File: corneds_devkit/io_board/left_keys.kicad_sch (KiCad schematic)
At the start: 64 parts, among them SW1 SW_Push, SW10 SW_Push, SW11 SW_Push, SW12 SW_Push, SW13 SW_Push, SW15 SW_Push, SW17 SW_Push, SW19 SW_Push, SW2 SW_Push, SW20 SW_Push, SW21 SW_Push, SW22 SW_Push, SW23 SW_Push, SW24 SW_Push, SW3 SW_Push, SW4 SW_Push, SW5 SW_Push, SW6 SW_Push, SW7 SW_Push, SW8 SW_Push, SW9 SW_Push

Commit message: finished mouse and key boards
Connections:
- net lclick_led_di: now reaches D38.1 (DO)
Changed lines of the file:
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@@
+	(wire
+		(pts
+			(xy 163.83 142.24) (xy 166.37 142.24)
+		)
+		(stroke
+			(width 0)
+			(type default)
+		)
+	)
 	(wire
 		(pts
@@
 				(hide yes)
 			)
+		)
+	)
+	(global_label "lclick_led_di"
+		(shape input)
+		(at 163.83 142.24 180)
+		(fields_autoplaced yes)
+		(effects
+			(font
+				(size 1.27 1.27)
+			)
+			(justify right)
+		)
+		(property "Intersheetrefs" "${INTERSHEET_REFS}"
+			(at 149.1125 142.24 0)
+			(effects
+				(font
+					(size 1.27 1.27)
+				)
+				(justify right)
+				(hide yes)
+			)

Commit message: finished schematic for io board
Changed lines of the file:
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@@
 	)
 	(junction
-		(at 255.27 152.4)
-		(diameter 0)
-		(color 0 0 0 0)
-	)
-	(junction
 		(at 229.87 152.4)
 		(diameter 0)
@@
 	)
 	(junction
-		(at 63.5 26.67)
-		(diameter 0)
-		(color 0 0 0 0)
-	)
-	(junction
 		(at 140.97 58.42)
 		(diameter 0)
@@
 		)
 	)
+	(global_label "VDDL"
+		(shape input)
+		(at 63.5 26.67 90)
+		(fields_autoplaced yes)
+		(effects
+			(font
+				(size 1.27 1.27)
+			)
+			(justify left)
+		)
+		(property "Intersheetrefs" "${INTERSHEET_REFS}"
+			(at 63.5 19.0281 90)
+			(effects
+				(font
+					(size 1.27 1.27)
+				)
+				(justify left)
+				(hide yes)
+			)
+		)
+	)
 	(global_label "key_t"
 		(shape input)
@@
 		)
 	)
+	(global_label "GNDL"
+		(shape input)
+		(at 255.27 152.4 270)
+		(fields_autoplaced yes)
+		(effects
+			(font
+				(size 1.27 1.27)
+			)
+			(justify right)
+		)
+		(property "Intersheetrefs" "${INTERSHEET_REFS}"
+			(at 255.27 160.2838 90)
+			(effects
+				(font
+					(size 1.27 1.27)
+				)
+				(justify right)
+				(hide yes)
+			)
+		)
+	)
 	(global_label "key_d"
 		(shape input)
@@
 	)
 	(symbol
-		(lib_id "power:VDD")
-		(at 63.5 26.67 0)
-		(unit 1)
-		(exclude_from_sim no)
-		(in_bom yes)
-		(on_board yes)
-		(dnp no)
-		(fields_autoplaced yes)
-		(property "Reference" "#PWR01"
-			(at 63.5 30.48 0)
-			(effects
-				(font
-					(size 1.27 1.27)
-				)
-				(hide yes)
-			)
-		)
-		(property "Value" "VDDL"
-			(at 63.5 21.59 0)
-			(effects
-				(font
-					(size 1.27 1.27)
-				)
-			)
-		)
-		(property "Footprint" ""
-			(at 63.5 26.67 0)
-			(effects
-				(font
-					(size 1.27 1.27)
-				)
-				(hide yes)
-			)
-		)
-		(property "Datasheet" ""
-			(at 63.5 26.67 0)
-			(effects
-				(font
-					(size 1.27 1.27)
-				)
-				(hide yes)
-			)
-		)
-		(property "Description" "Power symbol creates a global label with name \"VDD\""
-			(at 63.5 26.67 0)
-			(effects
-				(font
-					(size 1.27 1.27)
-				)
-				(hide yes)
-			)
-		)
-		(pin "1"
-		)
-		(instances
-			(project "io_board"
-				(path "/244b6d6b-132d-4d50-ae86-e41103b29008/035ff8de-23b0-4e40-a4d6-13420d9ceca3"
-					(reference "#PWR01")
-					(unit 1)
-				)
-			)
-		)
-	)
-	(symbol
 		(lib_id "Diode:1N4148W")
 		(at 156.21 100.33 180)
@@
 					(unit 1)
 				)
-			)
-		)
-	)
-	(symbol
-		(lib_id "power:GND")
-		(at 255.27 152.4 0)
-		(unit 1)
-		(exclude_from_sim no)
-		(in_bom yes)
-		(on_board yes)
-		(dnp no)
-		(fields_autoplaced yes)
-		(property "Reference" "#PWR02"
-			(at 255.27 158.75 0)
-			(effects
-				(font
-					(size 1.27 1.27)
-				)
-				(hide yes)
-			)
-		)
-		(property "Value" "GNDL"
-			(at 255.27 157.48 0)
-			(effects
-				(font
-					(size 1.27 1.27)
-				)
-			)
-		)
-		(property "Footprint" ""
-			(at 255.27 152.4 0)
-			(effects
-				(font
-					(size 1.27 1.27)
-				)
-				(hide yes)
-			)
-		)
-		(property "Datasheet" ""
-			(at 255.27 152.4 0)
-			(effects
-				(font
-					(size 1.27 1.27)
-				)
-				(hide yes)
-			)
-		)
-		(property "Description" "Power symbol creates a global label with name \"GND\" , ground"
-			(at 255.27 152.4 0)
-			(effects
-				(font
-					(size 1.27 1.27)
-				)
-				(hide yes)
-			)
-		)
-		(pin "1"
-		)
-		(instances
-			(project "io_board"
-				(path "/244b6d6b-132d-4d50-ae86-e41103b29008/035ff8de-23b0-4e40-a4d6-13420d9ceca3"
-					(reference "#PWR02")
-					(unit 1)
-				)

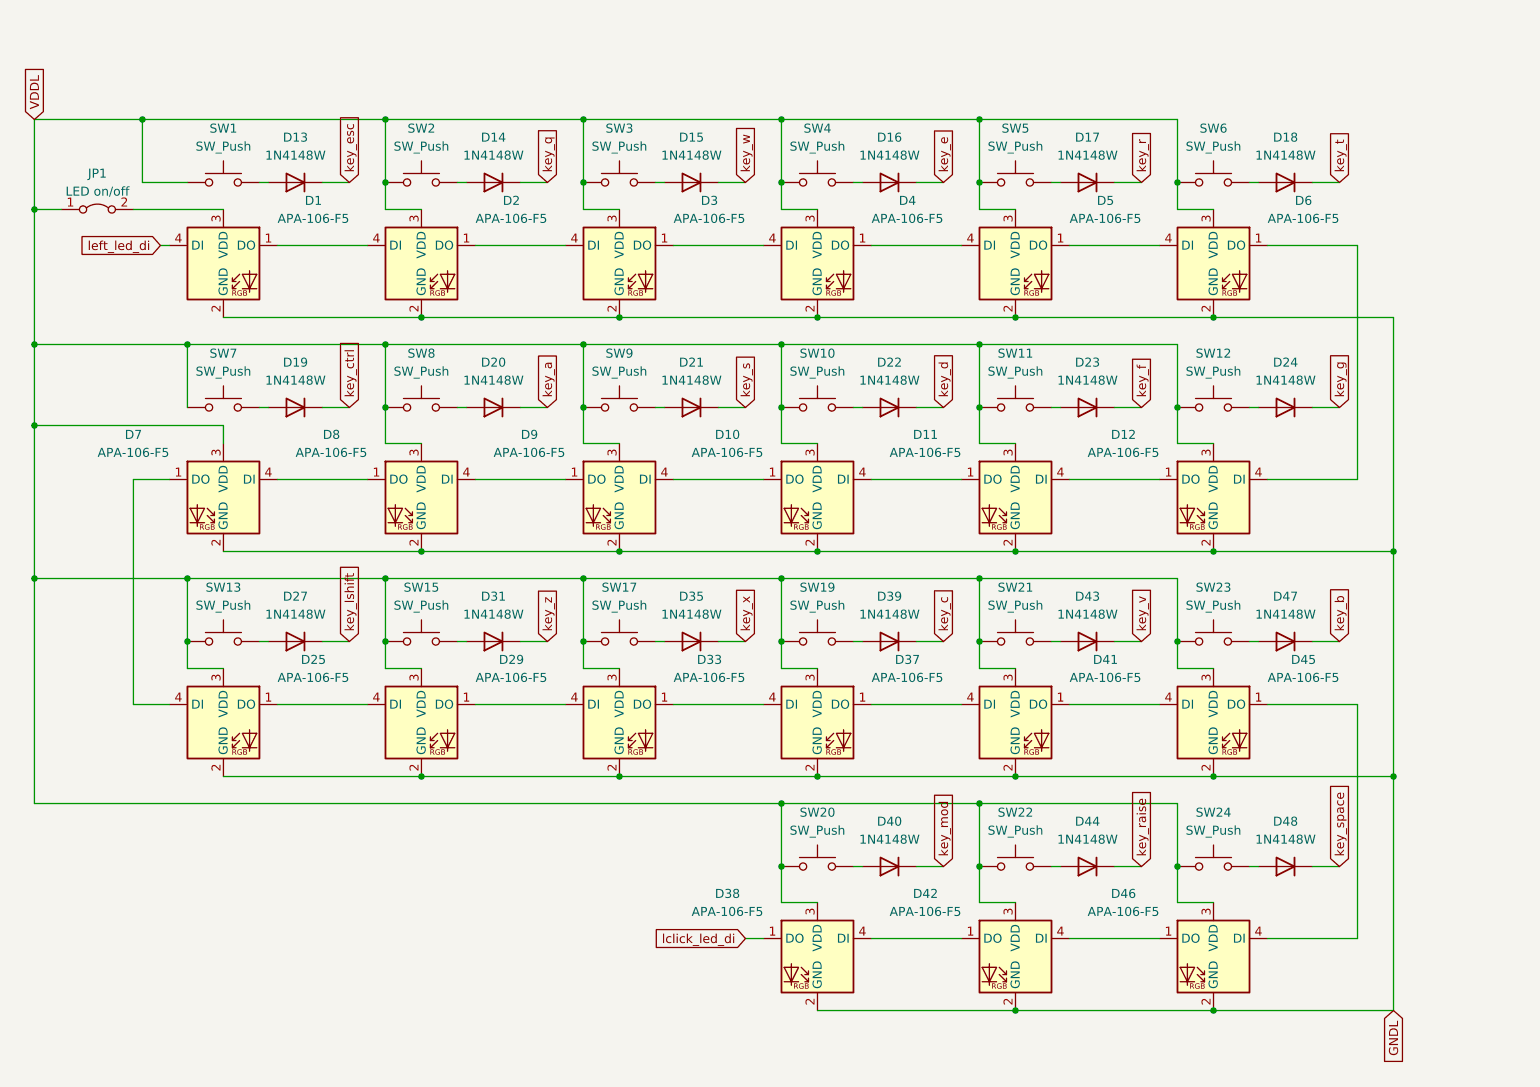
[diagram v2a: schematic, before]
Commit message: re-routed io board with keypad IC
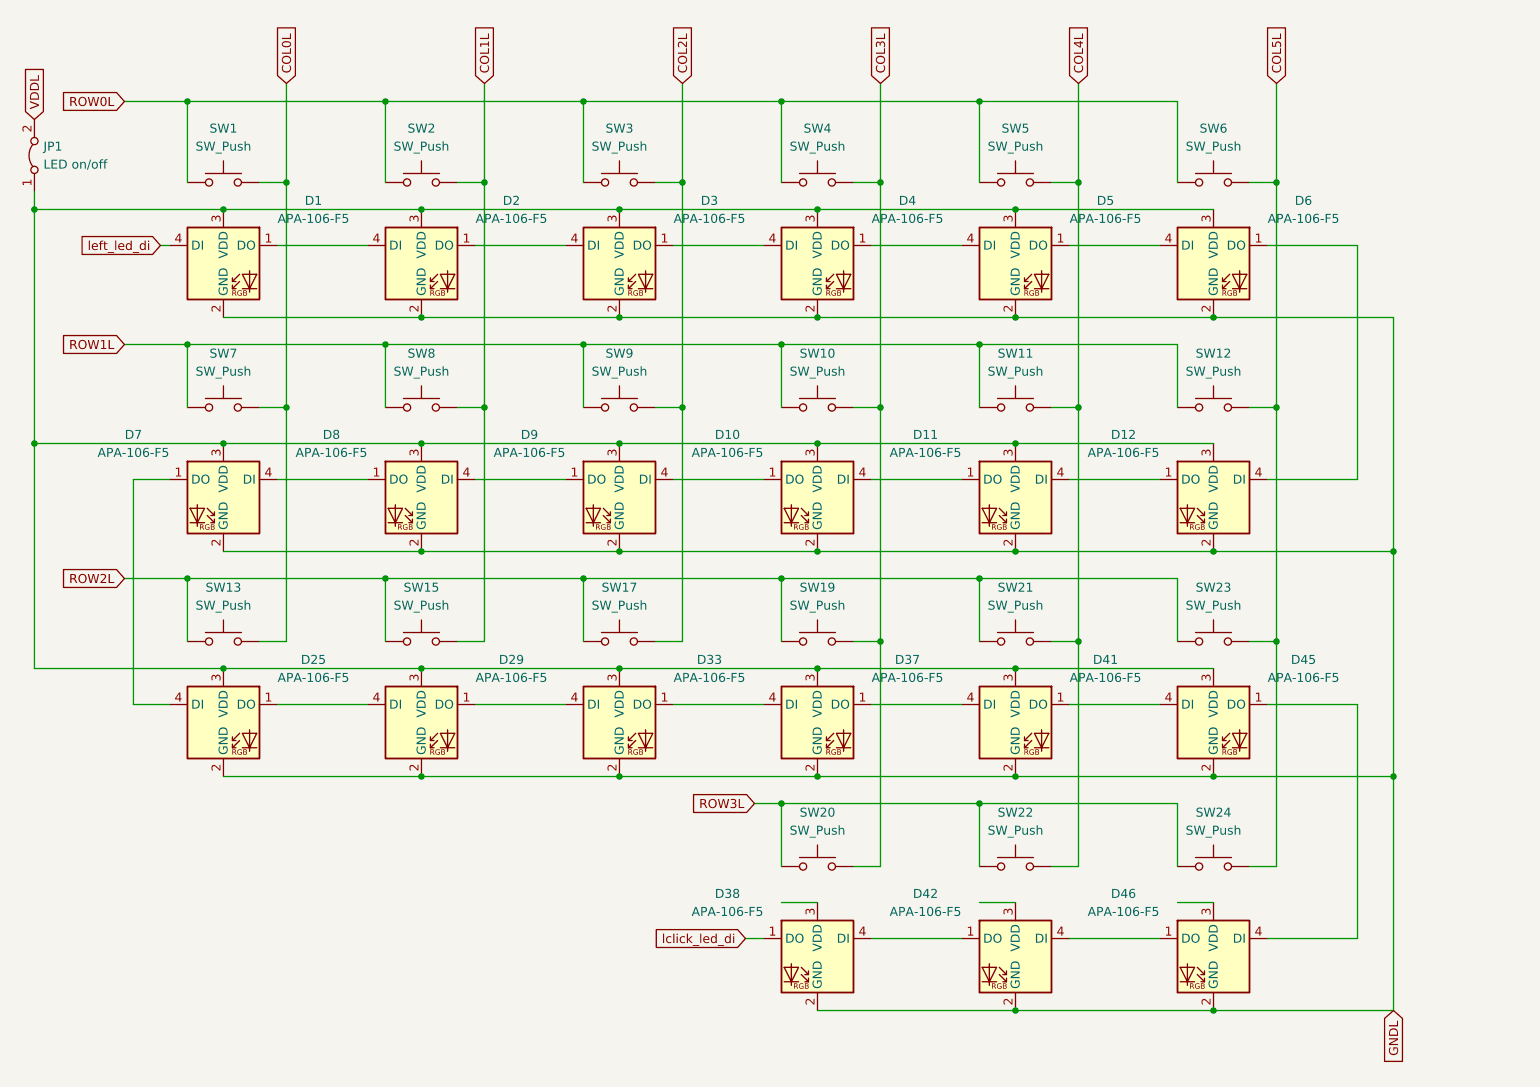
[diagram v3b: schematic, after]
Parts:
- removed D13, D14, D15, D16, D17, D18, D19, D20, D21, D22, D23, D24, D27, D31, D35, D39, D40, D43, D44, D47, D48: 1N4148W, Diode_SMD:D_SOD-123, symbol Diode:1N4148W
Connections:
- net VDDL: now also JP1.2 (B); no longer D10.3 (VDD), D11.3 (VDD), D12.3 (VDD), D2.3 (VDD), D25.3 (VDD), D29.3 (VDD), D3.3 (VDD), D33.3 (VDD), D37.3 (VDD), D38.3 (VDD), D4.3 (VDD), D41.3 (VDD), D42.3 (VDD), D45.3 (VDD), D46.3 (VDD), D5.3 (VDD), D6.3 (VDD), D7.3 (VDD), D8.3 (VDD), D9.3 (VDD), JP1.1 (A), SW1.1, SW10.1, SW11.1, SW12.1, SW13.1, SW15.1, SW17.1, SW19.1, SW2.1, SW20.1, SW21.1, SW22.1, SW23.1, SW24.1, SW3.1, SW4.1, SW5.1, SW6.1, SW7.1, SW8.1, SW9.1
- net COL4L: now reaches SW21.2
- net COL4L: now also SW11.2, SW22.2, SW5.2
- net COL5L: now reaches SW6.2
- net COL5L: now also SW12.2, SW23.2, SW24.2
- net COL3L: now reaches SW20.2
- net COL3L: now also SW10.2, SW19.2, SW4.2
- net at D1.3 (VDD): now also D10.3 (VDD), D11.3 (VDD), D12.3 (VDD), D2.3 (VDD), D25.3 (VDD), D29.3 (VDD), D3.3 (VDD), D33.3 (VDD), D37.3 (VDD), D4.3 (VDD), D41.3 (VDD), D45.3 (VDD), D5.3 (VDD), D6.3 (VDD), D7.3 (VDD), D8.3 (VDD), D9.3 (VDD), JP1.1 (A); no longer JP1.2 (B)
- net COL1L: now reaches SW8.2
- net COL1L: now also SW15.2, SW2.2
- net COL2L: now reaches SW3.2
- net COL2L: now also SW17.2, SW9.2
- net COL0L: now reaches SW7.2
- net COL0L: now also SW1.2, SW13.2
- new net ROW0L: SW1.1, SW2.1, SW3.1, SW4.1, SW5.1, SW6.1
- new net ROW1L: SW10.1, SW11.1, SW12.1, SW7.1, SW8.1, SW9.1
- new net ROW2L: SW13.1, SW15.1, SW17.1, SW19.1, SW21.1, SW23.1
- new net ROW3L: SW20.1, SW22.1, SW24.1
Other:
- moved on the sheet: JP1

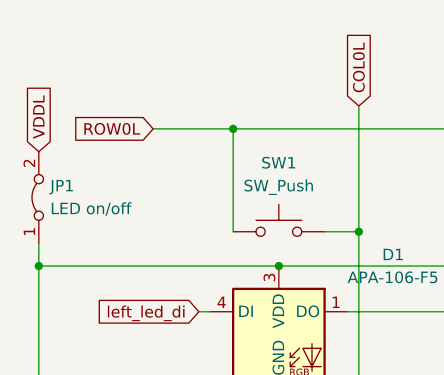
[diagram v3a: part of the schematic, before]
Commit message: added switch footprint, io sch, and keypad IC footprint. Need to find new LEDs and make joystick footprint
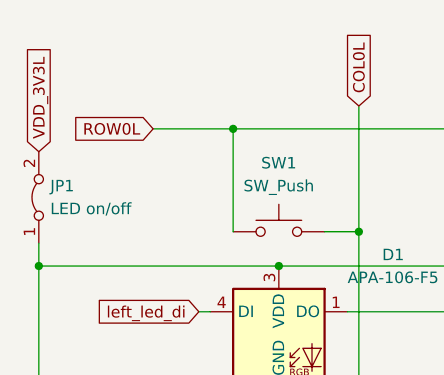
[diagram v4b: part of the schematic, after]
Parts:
- SW1, SW10, SW11, SW12, SW13, SW15, SW17, SW19, SW2, SW20, SW21, SW22, SW23, SW24, SW3, SW4, SW5, SW6, SW7, SW8, SW9: footprint (none) -> key-switches:SW_Gateron_LowProfile_HotSwap_THT
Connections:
- net VDDL renamed VDD_3V3L
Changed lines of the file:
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@@
 		)
 	)
-	(global_label "VDDL"
+	(global_label "VDD_3V3L"
 		(shape input)
 		(at 63.5 26.67 90)
@@
 		)
 		(property "Intersheetrefs" "${INTERSHEET_REFS}"
-			(at 63.5 19.0281 90)
+			(at 63.5 14.5529 90)
 			(effects
 				(font
@@
 			)
 		)
-		(property "Footprint" ""
+		(property "Footprint" "key-switches:SW_Gateron_LowProfile_HotSwap_THT"
 			(at 201.93 95.25 0)
 			(effects
@@
 			)
 		)
-		(property "Footprint" ""
+		(property "Footprint" "key-switches:SW_Gateron_LowProfile_HotSwap_THT"
 			(at 229.87 30.48 0)
 			(effects
@@
 			)
 		)
-		(property "Footprint" ""
+		(property "Footprint" "key-switches:SW_Gateron_LowProfile_HotSwap_THT"
 			(at 173.99 127 0)
 			(effects
@@
 			)
 		)
-		(property "Footprint" ""
+		(property "Footprint" "key-switches:SW_Gateron_LowProfile_HotSwap_THT"
 			(at 173.99 62.23 0)
 			(effects
@@
 			)
 		)
-		(property "Footprint" ""
+		(property "Footprint" "key-switches:SW_Gateron_LowProfile_HotSwap_THT"
 			(at 118.11 62.23 0)
 			(effects
@@
 			)
 		)
-		(property "Footprint" ""
+		(property "Footprint" "key-switches:SW_Gateron_LowProfile_HotSwap_THT"
 			(at 173.99 95.25 0)
 			(effects
@@
 			)
 		)
-		(property "Footprint" ""
+		(property "Footprint" "key-switches:SW_Gateron_LowProfile_HotSwap_THT"
 			(at 229.87 95.25 0)
 			(effects
@@
 			)
 		)
-		(property "Footprint" ""
+		(property "Footprint" "key-switches:SW_Gateron_LowProfile_HotSwap_THT"
 			(at 90.17 62.23 0)
 			(effects
@@
 			)
 		)
-		(property "Footprint" ""
+		(property "Footprint" "key-switches:SW_Gateron_LowProfile_HotSwap_THT"
 			(at 90.17 30.48 0)
 			(effects
@@
 			)
 		)
-		(property "Footprint" ""
+		(property "Footprint" "key-switches:SW_Gateron_LowProfile_HotSwap_THT"
 			(at 229.87 62.23 0)
 			(effects
@@
 			)
 		)
-		(property "Footprint" ""
+		(property "Footprint" "key-switches:SW_Gateron_LowProfile_HotSwap_THT"
 			(at 173.99 30.48 0)
 			(effects
@@
 			)
 		)
-		(property "Footprint" ""
+		(property "Footprint" "key-switches:SW_Gateron_LowProfile_HotSwap_THT"
 			(at 201.93 30.48 0)
 			(effects
@@
 			)
 		)
-		(property "Footprint" ""
+		(property "Footprint" "key-switches:SW_Gateron_LowProfile_HotSwap_THT"
 			(at 201.93 62.23 0)
 			(effects
@@
 			)
 		)
-		(property "Footprint" ""
+		(property "Footprint" "key-switches:SW_Gateron_LowProfile_HotSwap_THT"
 			(at 146.05 95.25 0)
 			(effects
@@
 			)
 		)
-		(property "Footprint" ""
+		(property "Footprint" "key-switches:SW_Gateron_LowProfile_HotSwap_THT"
 			(at 201.93 127 0)
 			(effects
@@
 			)
 		)
-		(property "Footprint" ""
+		(property "Footprint" "key-switches:SW_Gateron_LowProfile_HotSwap_THT"
 			(at 118.11 95.25 0)
 			(effects
@@
 			)
 		)
-		(property "Footprint" ""
+		(property "Footprint" "key-switches:SW_Gateron_LowProfile_HotSwap_THT"
 			(at 90.17 95.25 0)
 			(effects
@@
 			)
 		)
-		(property "Footprint" ""
+		(property "Footprint" "key-switches:SW_Gateron_LowProfile_HotSwap_THT"
 			(at 118.11 30.48 0)
 			(effects
@@
 			)
 		)
-		(property "Footprint" ""
+		(property "Footprint" "key-switches:SW_Gateron_LowProfile_HotSwap_THT"
 			(at 146.05 62.23 0)
 			(effects
@@
 			)
 		)
-		(property "Footprint" ""
+		(property "Footprint" "key-switches:SW_Gateron_LowProfile_HotSwap_THT"
 			(at 146.05 30.48 0)
 			(effects
@@
 			)
 		)
-		(property "Footprint" ""
+		(property "Footprint" "key-switches:SW_Gateron_LowProfile_HotSwap_THT"
 			(at 229.87 127 0)
 			(effects

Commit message: io sch done. Need to route
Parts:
- removed JP1: LED on/off, symbol Jumper:Jumper_2_Bridged
- D1, D10, D11, D12, D2, D25, D29, D3, D33, D37, D38, D4, D41, D42, D45, D46, D5, D6, D7, D8, D9: value APA-106-F5 -> SK68XX-SIDE; footprint LED_THT:LED_D5.0mm-4_RGB -> entropy:SK68XX-SIDE
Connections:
- net VDD_5VL: now reaches D1.3 (VDD), D10.3 (VDD), D11.3 (VDD), D12.3 (VDD), D2.3 (VDD), D25.3 (VDD), D29.3 (VDD), D3.3 (VDD), D33.3 (VDD), D37.3 (VDD), D4.3 (VDD), D41.3 (VDD), D45.3 (VDD), D5.3 (VDD), D6.3 (VDD), D7.3 (VDD), D8.3 (VDD), D9.3 (VDD)
- net VDD_5VL: now also D38.3 (VDD), D42.3 (VDD), D46.3 (VDD)
